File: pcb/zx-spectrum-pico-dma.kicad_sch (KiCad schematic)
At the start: 19 parts, among them J101 SWD, J102 Blippers, J103 Z80 Data Bus, J104 Z80 Address Bus, J105 Z80 Control Bus, J106 ZX Control, J107 OLED, J108 Spare GPIOs, Q101 PMBT2222A, SW101 BTN_RESET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

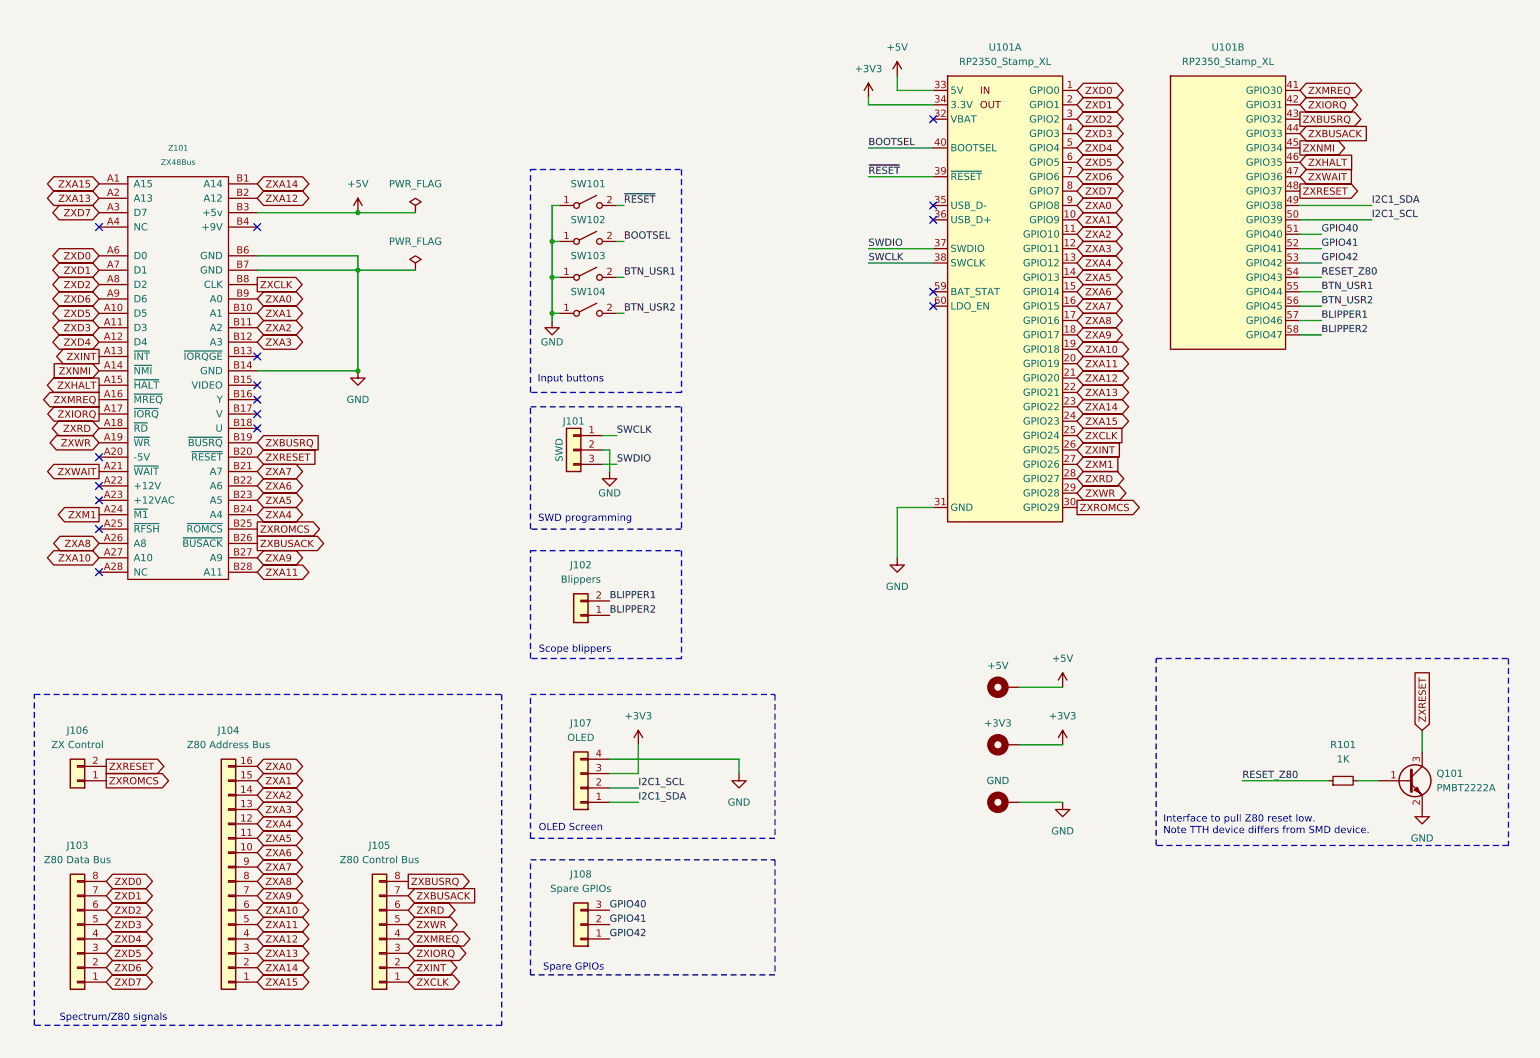
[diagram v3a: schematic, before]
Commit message: thought about barrel jacks to control zx power, decided against. final tidyups
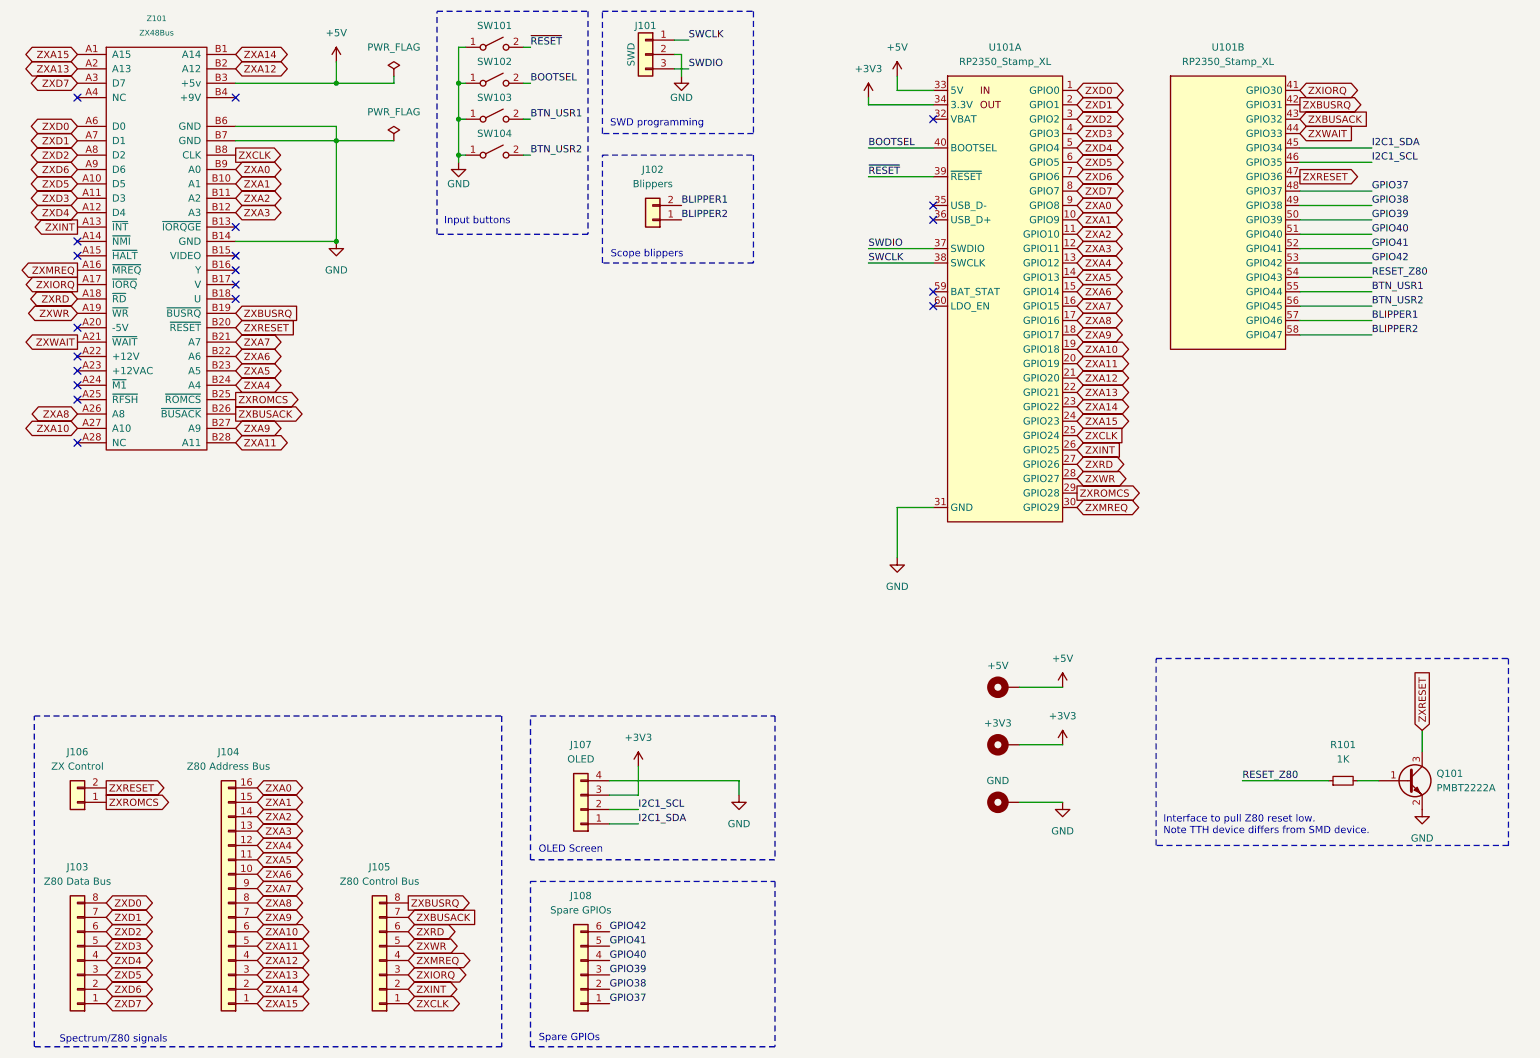
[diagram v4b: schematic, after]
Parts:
- J108: footprint Connector_PinHeader_2.54mm:PinHeader_1x03_P2.54mm_Vertical -> Connector_PinHeader_2.54mm:PinHeader_1x06_P2.54mm_Vertical; symbol Connector_Generic:Conn_01x03 -> Connector_Generic:Conn_01x06
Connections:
- net GPIO40: now also J108.4 (Pin_4); no longer J108.3 (Pin_3)
- net GPIO41: now also J108.5 (Pin_5); no longer J108.2 (Pin_2)
- net GPIO42: now also J108.6 (Pin_6); no longer J108.1 (Pin_1)
- net I2C1_SCL: now also U101.46 (GPIO35); no longer U101.50 (GPIO39)
- net I2C1_SDA: now also U101.45 (GPIO34); no longer U101.49 (GPIO38)
- net ZXBUSACK: now also U101.43 (GPIO32); no longer U101.44 (GPIO33)
- net ZXBUSRQ: now also U101.42 (GPIO31); no longer U101.43 (GPIO32)
- net ZXIORQ: now also U101.41 (GPIO30); no longer U101.42 (GPIO31)
- net ZXMREQ: now also U101.30 (GPIO29); no longer U101.41 (GPIO30)
- net ZXRD: now also U101.27 (GPIO26); no longer U101.28 (GPIO27)
- net ZXRESET: now also U101.47 (GPIO36); no longer U101.48 (GPIO37)
- net ZXROMCS: now also U101.29 (GPIO28); no longer U101.30 (GPIO29)
- net ZXWAIT: now also U101.44 (GPIO33); no longer U101.47 (GPIO36)
- net ZXWR: now also U101.28 (GPIO27); no longer U101.29 (GPIO28)
- net ZXHALT: no longer names the net of Z101.A15 (~{HALT})
- net ZXHALT: no longer U101.46 (GPIO35)
- net ZXM1: no longer names the net of Z101.A24 (~{M1})
- net ZXM1: no longer U101.27 (GPIO26)
- net ZXNMI: no longer names the net of Z101.A14 (~{NMI})
- net ZXNMI: no longer U101.45 (GPIO34)
- new net GPIO37: J108.1 (Pin_1), U101.48 (GPIO37)
- new net GPIO38: J108.2 (Pin_2), U101.49 (GPIO38)
- new net GPIO39: J108.3 (Pin_3), U101.50 (GPIO39)
- no-connect marks 17 -> 20
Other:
- moved on the sheet: J101, J102, J103, J104, J105, J106, J107, SW101, SW102, SW103, SW104, Z101

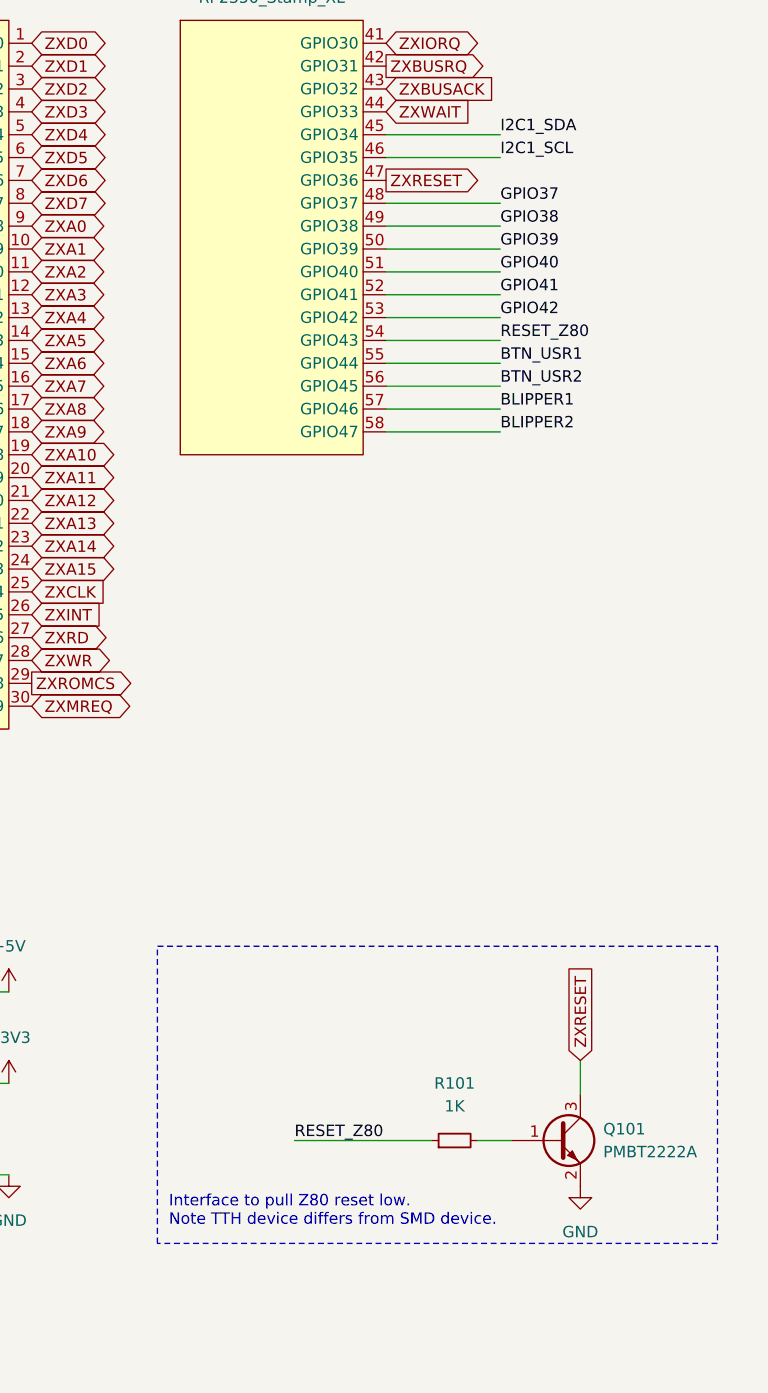
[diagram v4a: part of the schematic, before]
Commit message: update schematic to reflect the revised RESET labelling
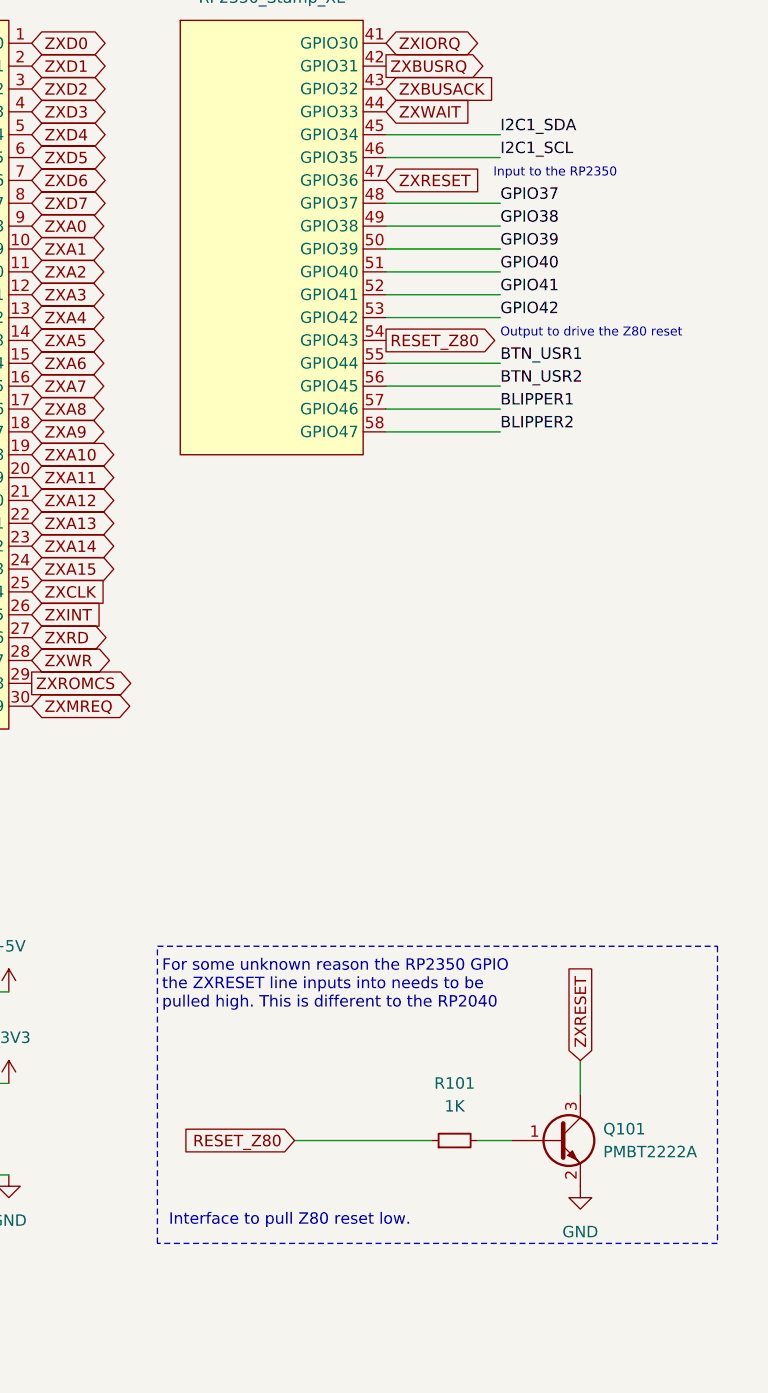
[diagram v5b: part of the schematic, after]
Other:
- note added: "For some unknown reason the RP2350 GPIO the ZXRESET line inputs into needs to be pulled high. This is different to the RP2040"
- note added: "Input to the RP2350"
- note added: "Interface to pull Z80 reset low."
- note added: "Output to drive the Z80 reset"
- note removed: "Interface to pull Z80 reset low. Note TTH device differs from SMD device."
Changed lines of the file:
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@@
 	(title_block
 		(title "RP2350B Spectrum DMA Interface")
-		(date "2024-11-29")
+		(date "2025-02-26")
 	)
 	(junction
@@
 	(wire
 		(pts
-			(xy 242.57 60.96) (xy 255.27 60.96)
-		)
-		(stroke
-			(width 0)
-			(type default)
-		)
-	)
-	(wire
-		(pts
 			(xy 95.25 20.32) (xy 93.98 20.32)
 		)
@@
 		)
 	)
+	(text "Input to the RP2350"
+		(exclude_from_sim no)
+		(at 261.366 42.418 0)
+		(effects
+			(font
+				(size 1 1)
+			)
+		)
+	)
 	(text "Input buttons"
 		(exclude_from_sim no)
@@
 		)
 	)
+	(text "For some unknown reason the RP2350 GPIO\nthe ZXRESET line inputs into needs to be\npulled high. This is different to the RP2040"
+		(exclude_from_sim no)
+		(at 217.678 132.588 0)
+		(effects
+			(font
+				(size 1.27 1.27)
+			)
+			(justify left)
+		)
+	)
 	(text "Spare GPIOs"
 		(exclude_from_sim no)
@@
 		)
 	)
-	(text "Interface to pull Z80 reset low.\nNote TTH device differs from SMD device."
+	(text "Interface to pull Z80 reset low."
 		(exclude_from_sim no)
 		(at 218.44 159.512 0)
@@
 		)
 	)
+	(text "Output to drive the Z80 reset"
+		(exclude_from_sim no)
+		(at 255.27 60.198 0)
+		(effects
+			(font
+				(size 1 1)
+			)
+			(justify left)
+		)
+	)
 	(text "SWD programming"
 		(exclude_from_sim no)
@@
 	(label "GPIO39"
 		(at 120.65 184.15 0)
-		(fields_autoplaced yes)
 		(effects
 			(font
@@
 	(label "GPIO42"
 		(at 255.27 58.42 0)
-		(fields_autoplaced yes)
 		(effects
 			(font
@@
 	(label "I2C1_SDA"
 		(at 255.27 38.1 0)
-		(fields_autoplaced yes)
 		(effects
 			(font
@@
 	(label "GPIO38"
 		(at 255.27 48.26 0)
-		(fields_autoplaced yes)
 		(effects
 			(font
@@
 	(label "BOOTSEL"
 		(at 106.68 26.67 0)
-		(fields_autoplaced yes)
 		(effects
 			(font
@@
 	(label "~{RESET}"
 		(at 166.37 43.18 0)
-		(fields_autoplaced yes)
 		(effects
 			(font
@@
 	(label "BLIPPER2"
 		(at 255.27 71.12 0)
-		(fields_autoplaced yes)
 		(effects
 			(font
@@
 	(label "GPIO40"
 		(at 120.65 181.61 0)
-		(fields_autoplaced yes)
 		(effects
 			(font
@@
 	(label "GPIO40"
 		(at 255.27 53.34 0)
-		(fields_autoplaced yes)
 		(effects
 			(font
@@
 	(label "GPIO41"
 		(at 120.65 179.07 0)
-		(fields_autoplaced yes)
 		(effects
 			(font
@@
 	(label "I2C1_SDA"
 		(at 125.73 157.48 0)
-		(fields_autoplaced yes)
 		(effects
 			(font
@@
 	(label "SWCLK"
 		(at 134.62 19.05 0)
-		(fields_autoplaced yes)
 		(effects
 			(font
@@
 	(label "BLIPPER1"
 		(at 255.27 68.58 0)
-		(fields_autoplaced yes)
 		(effects
 			(font
@@
 	(label "BLIPPER1"
 		(at 133.35 48.26 0)
-		(fields_autoplaced yes)
 		(effects
 			(font
@@
 	(label "BOOTSEL"
 		(at 166.37 38.1 0)
-		(fields_autoplaced yes)
-		(effects
-			(font
-				(size 1.27 1.27)
-			)
-			(justify left bottom)
-		)
-	)
-	(label "RESET_Z80"
-		(at 232.41 149.86 0)
-		(fields_autoplaced yes)
-		(effects
-			(font
-				(size 1.27 1.27)
-			)
-			(justify left bottom)
-		)
-	)
-	(label "RESET_Z80"
-		(at 255.27 60.96 0)
-		(fields_autoplaced yes)
 		(effects
 			(font
@@
 	(label "GPIO41"
 		(at 255.27 55.88 0)
-		(fields_autoplaced yes)
 		(effects
 			(font
@@
 	(label "SWDIO"
 		(at 166.37 55.88 0)
-		(fields_autoplaced yes)
 		(effects
 			(font
@@
 	(label "GPIO39"
 		(at 255.27 50.8 0)
-		(fields_autoplaced yes)
 		(effects
 			(font
@@
 	(label "I2C1_SCL"
 		(at 255.27 40.64 0)
-		(fields_autoplaced yes)
 		(effects
 			(font
@@
 	(label "BLIPPER2"
 		(at 133.35 50.8 0)
-		(fields_autoplaced yes)
 		(effects
 			(font
@@
 	(label "GPIO42"
 		(at 120.65 176.53 0)
-		(fields_autoplaced yes)
 		(effects
 			(font
@@
 	(label "BTN_USR1"
 		(at 106.68 33.02 0)
-		(fields_autoplaced yes)
 		(effects
 			(font
@@
 	(label "SWDIO"
 		(at 134.62 24.13 0)
-		(fields_autoplaced yes)
 		(effects
 			(font
@@
 	(label "SWCLK"
 		(at 166.37 58.42 0)
-		(fields_autoplaced yes)
 		(effects
 			(font
@@
 	(label "BTN_USR2"
 		(at 255.27 66.04 0)
-		(fields_autoplaced yes)
 		(effects
 			(font
@@
 	(label "GPIO37"
 		(at 255.27 45.72 0)
-		(fields_autoplaced yes)
 		(effects
 			(font
@@
 	(label "~{RESET}"
 		(at 106.68 20.32 0)
-		(fields_autoplaced yes)
 		(effects
 			(font
@@
 	(label "BTN_USR2"
 		(at 106.68 39.37 0)
-		(fields_autoplaced yes)
 		(effects
 			(font
@@
 	(label "GPIO38"
 		(at 120.65 186.69 0)
-		(fields_autoplaced yes)
 		(effects
 			(font
@@
 	(label "BTN_USR1"
 		(at 255.27 63.5 0)
-		(fields_autoplaced yes)
 		(effects
 			(font
@@
 	(label "GPIO37"
 		(at 120.65 189.23 0)
-		(fields_autoplaced yes)
 		(effects
 			(font
@@
 	(label "I2C1_SCL"
 		(at 125.73 154.94 0)
-		(fields_autoplaced yes)
 		(effects
 			(font
@@
 		)
 	)
+	(global_label "RESET_Z80"
+		(shape output)
+		(at 242.57 60.96 0)
+		(fields_autoplaced yes)
+		(effects
+			(font
+				(size 1.27 1.27)
+			)
+			(justify left)
+		)
+		(property "Intersheetrefs" "${INTERSHEET_REFS}"
+			(at 255.8964 60.96 0)
+			(effects
+				(font
+					(size 1.27 1.27)
+				)
+				(justify left)
+				(hide yes)
+			)
+		)
+	)
 	(global_label "ZXBUSACK"
 		(shape input)
@@
 	)
 	(global_label "ZXRESET"
-		(shape output)
+		(shape input)
 		(at 242.57 43.18 0)
 		(fields_autoplaced yes)
@@
 				(hide yes)
 			)
+		)
+	)
+	(global_label "RESET_Z80"
+		(shape input)
+		(at 232.41 149.86 180)
+		(fields_autoplaced yes)
+		(effects
+			(font
+				(size 1.27 1.27)
+			)
+			(justify right)
+		)
+		(property "Intersheetrefs" "${INTERSHEET_REFS}"
+			(at 219.0836 149.86 0)
+			(effects
+				(font
+					(size 1.27 1.27)
+				)
+				(justify right)
+				(hide yes)
+			)
